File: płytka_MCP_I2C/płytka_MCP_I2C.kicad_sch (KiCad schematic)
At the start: 32 parts, among them J1 A0, J10 V0, J11 Ext, J12 I2C, J14 U1, J15 U2, J16 U3, J17 RS, J18 K, J19 A, J2 A1, J20 VDD, J21 GND, J23 VSS, J24 Conn_01x16_Pin, J25 LCD, J26 VCC, J3 A2, J4 SDA, J5 SCL, J6 INTA, J7 INTB, J8 INTA, U1 MCP23017_SP

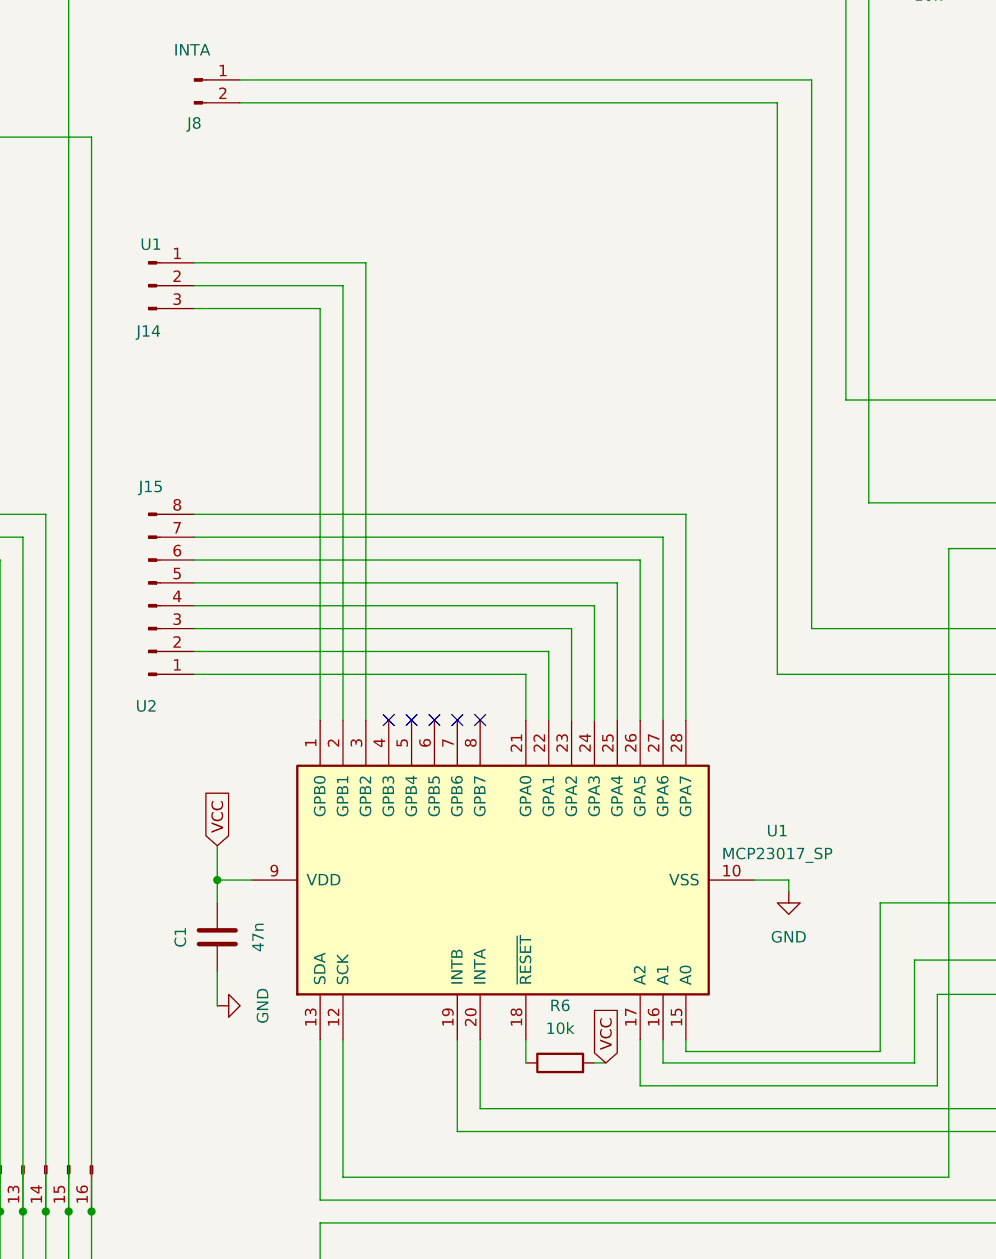
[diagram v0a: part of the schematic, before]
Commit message: Dodany pin RESET
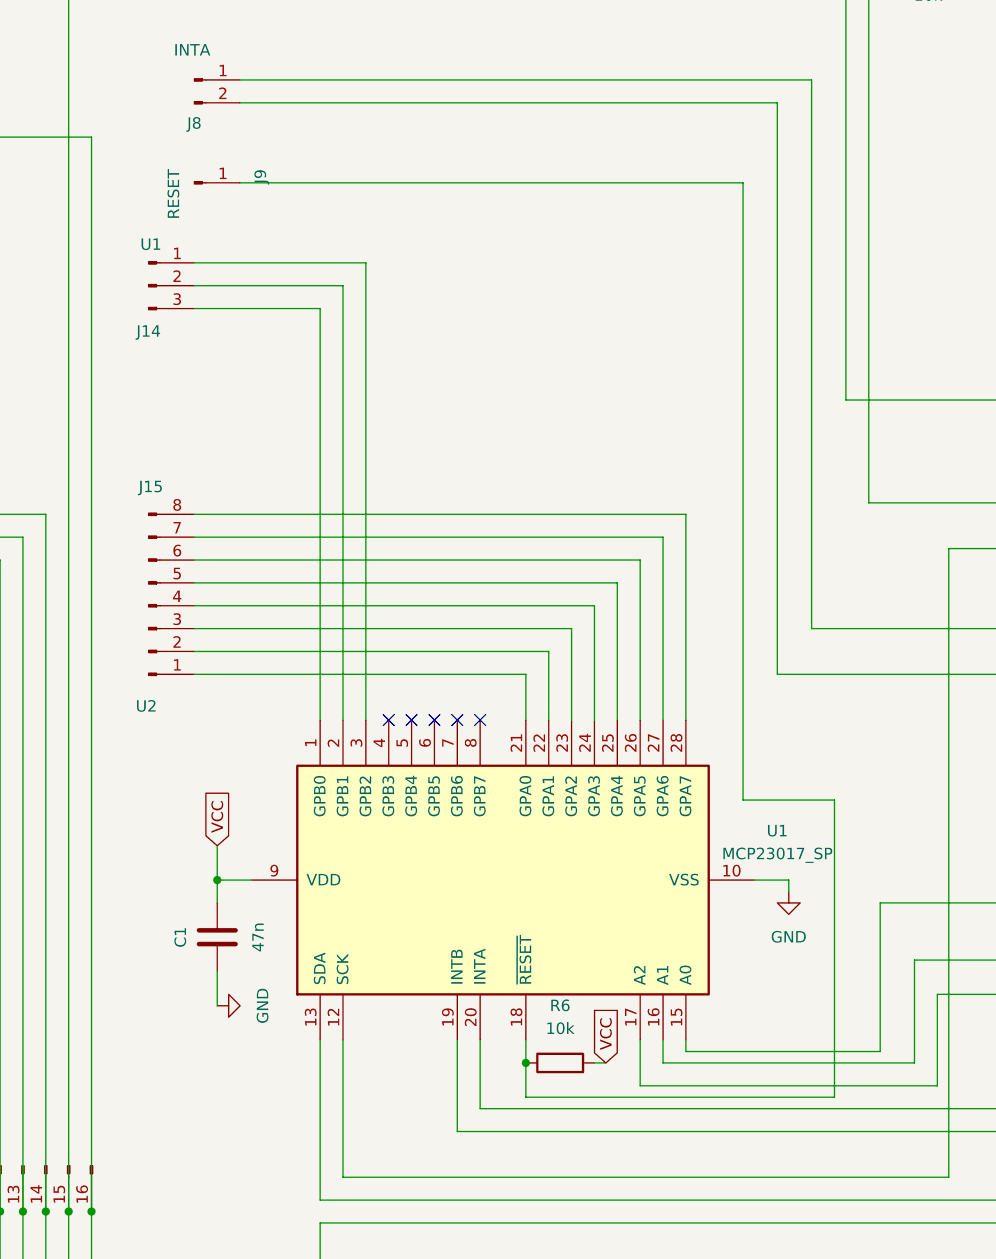
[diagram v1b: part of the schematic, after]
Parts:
- added J9: RESET, Connector_PinSocket_2.54mm:PinSocket_1x01_P2.54mm_Vertical, symbol Connector:Conn_01x01_Pin
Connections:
- net at R6.1, U1.18 (~{RESET}): now also J9.1 (Pin_1)
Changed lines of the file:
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@@
 	)
 	(junction
+		(at 157.48 146.05)
+		(diameter 0)
+		(color 0 0 0 0)
+	)
+	(junction
 		(at 236.22 83.82)
 		(diameter 0)
@@
 	(wire
 		(pts
+			(xy 181.61 48.26) (xy 181.61 116.84)
+		)
+		(stroke
+			(width 0)
+			(type default)
+		)
+	)
+	(wire
+		(pts
 			(xy 73.66 39.37) (xy 68.58 39.37)
 		)
@@
 	(wire
 		(pts
+			(xy 191.77 149.86) (xy 157.48 149.86)
+		)
+		(stroke
+			(width 0)
+			(type default)
+		)
+	)
+	(wire
+		(pts
 			(xy 218.44 43.18) (xy 219.71 43.18)
 		)
@@
 	(wire
 		(pts
+			(xy 125.73 48.26) (xy 181.61 48.26)
+		)
+		(stroke
+			(width 0)
+			(type default)
+		)
+	)
+	(wire
+		(pts
 			(xy 233.68 88.9) (xy 233.68 83.82)
 		)
@@
 	(wire
 		(pts
+			(xy 181.61 116.84) (xy 191.77 116.84)
+		)
+		(stroke
+			(width 0)
+			(type default)
+		)
+	)
+	(wire
+		(pts
 			(xy 91.44 162.56) (xy 91.44 97.79)
 		)
@@
 	(wire
 		(pts
+			(xy 191.77 116.84) (xy 191.77 149.86)
+		)
+		(stroke
+			(width 0)
+			(type default)
+		)
+	)
+	(wire
+		(pts
 			(xy 224.79 68.58) (xy 224.79 80.01)
 		)
@@
 	(wire
 		(pts
+			(xy 157.48 146.05) (xy 157.48 149.86)
+		)
+		(stroke
+			(width 0)
+			(type default)
+		)
+	)
+	(wire
+		(pts
 			(xy 267.97 142.24) (xy 267.97 149.86)
 		)
@@
 					(unit 1)
 				)
+			)
+		)
+	)
+	(symbol
+		(lib_id "Connector:Conn_01x01_Pin")
+		(at 120.65 48.26 0)
+		(unit 1)
+		(exclude_from_sim no)
+		(in_bom yes)
+		(on_board yes)
+		(dnp no)
+		(property "Reference" "J9"
+			(at 128.016 46.736 90)
+			(effects
+				(font
+					(size 1.27 1.27)
+				)
+				(justify right)
+			)
+		)
+		(property "Value" "RESET"
+			(at 118.364 46.736 90)
+			(effects
+				(font
+					(size 1.27 1.27)
+				)
+				(justify right)
+			)
+		)
+		(property "Footprint" "Connector_PinSocket_2.54mm:PinSocket_1x01_P2.54mm_Vertical"
+			(at 120.65 48.26 0)
+			(effects
+				(font
+					(size 1.27 1.27)
+				)
+				(hide yes)
+			)
+		)
+		(property "Datasheet" "~"
+			(at 120.65 48.26 0)
+			(effects
+				(font
+					(size 1.27 1.27)
+				)
+				(hide yes)
+			)
+		)
+		(property "Description" "Generic connector, single row, 01x01, script generated"
+			(at 120.65 48.26 0)
+			(effects
+				(font
+					(size 1.27 1.27)
+				)
+				(hide yes)
+			)
+		)
+		(pin "1"
+		)
+		(instances
+			(project "płytka_MCP_I2C"
+				(path "/3b722ef3-3e65-45b1-8f17-63d4069d1a23"
+					(reference "J9")
+					(unit 1)
+				)
